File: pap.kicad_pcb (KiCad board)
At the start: 2 copper layers, 60 x 60 mm, 72 parts, among them J51 Conn_01x04, J52 Conn_01x02, J53 Conn_01x02, J54 RJ45, J55 RJ45, J56 RJ12, U1 powerstep01

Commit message: agreo fabricante y algun detalle menor en pcb
solo agrego unos detalles en fab de pcb indicando vias, pistas y
tecnologia de fabricacion. algo tenia, completo algun detalle mas
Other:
- board text added: "AllPCB Fab ********************************** Silkscreen Top White ------------------------- Solder Mask Top Green ------------------------- TOP 2Oz HASL ------------------------- FR4 1.6mm ------------------------- Bottom 2 Oz HASL ------------------------- Solder Mask Bottom Green ------------------------- Silkscreen Bottom White ------------------------- Paste Mask Bottom *********************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"
- board text removed: "Paste Mask Top ------------------------- Silkscreen Top ------------------------- Solder Mask Top ------------------------- TOP 2Oz ------------------------- FR4 1.6mm ------------------------- Bottom 2 Oz ------------------------- Solder Mask Bottom ------------------------- Silkscreen Bottom ------------------------- Paste Mask Bottom -------------------------"
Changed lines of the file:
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@@
   )
   (setup
-    (last_trace_width 1)
+    (last_trace_width 0.2)
     (user_trace_width 0.2)
     (user_trace_width 0.4)
@@
   (gr_line (start 90.83031 137.749079) (end 154.83031 137.749079) (layer Eco2.User) (width 0.3))
   (gr_line (start 90.83031 87.749079) (end 90.83031 137.749079) (layer Eco2.User) (width 0.3))
-  (gr_text "Paste Mask Top\n-------------------------\nSilkscreen Top\n-------------------------\nSolder Mask Top\n-------------------------\nTOP 2Oz\n-------------------------\nFR4 1.6mm\n-------------------------\nBottom 2 Oz\n-------------------------\nSolder Mask Bottom\n-------------------------\nSilkscreen Bottom\n-------------------------\nPaste Mask Bottom\n-------------------------" (at 188.18031 113.579079) (layer F.Fab)
+  (gr_text "AllPCB Fab\n**********************************\n\n\nSilkscreen Top White\n-------------------------\nSolder Mask Top Green\n-------------------------\nTOP 2Oz HASL\n-------------------------\nFR4 1.6mm\n-------------------------\nBottom 2 Oz HASL\n-------------------------\nSolder Mask Bottom Green\n-------------------------\nSilkscreen Bottom White\n-------------------------\nPaste Mask Bottom\n\n**************************************\nTrace/space = 0.25/0.25 mm\n**************************************\nVias Drill/Pad = 0.4/0.8mm\n**************************************" (at 187.23031 112.149079) (layer F.Fab)
     (effects (font (size 1.5 1.5) (thickness 0.3)) (justify left))
   )

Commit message: reviso y ajusto minimo track global a 0.25
en realidad el iC requiere de track de 0.2, pero el resto de la placa
intento llegar a 0.25 para tecnologia de 10/10 mils, y generalmente se
acepta que para el integrado sea un poco mayor que para el ruteo.
veremos.. lo dejo en 0.25/0.25
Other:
- net class Default: trace_width 0.2 -> 0.25
- rule trace_min: 0.2 -> 0.25
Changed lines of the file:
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@@
   )
   (setup
-    (last_trace_width 0.2)
-    (user_trace_width 0.2)
+    (last_trace_width 0.25)
+    (user_trace_width 0.25)
     (user_trace_width 0.4)
     (user_trace_width 0.8)
@@
     (zone_clearance 0.8)
     (zone_45_only yes)
-    (trace_min 0.2)
+    (trace_min 0.25)
     (segment_width 0.3)
     (edge_width 0.15)
@@
   (net_class Default "This is the default net class."
     (clearance 0.25)
-    (trace_width 0.2)
+    (trace_width 0.25)
     (via_dia 1)
     (via_drill 0.5)

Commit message: agfego valores faltantes de capas
Gracias al aporte de Gonzalo, me habian quedado algunos capas sin valor.
.Corrijo. Hay otras sugerencias de Gonzalo que no se corrigen, solo se
consideran y se evaluaran luego
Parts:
- C10, C11, C2, C7, C8: value C -> 100n
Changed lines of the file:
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@@
   (layers
     (0 F.Cu signal)
-    (31 B.Cu signal)
+    (31 B.Cu signal hide)
     (32 B.Adhes user hide)
     (33 F.Adhes user hide)
     (34 B.Paste user hide)
     (35 F.Paste user hide)
-    (36 B.SilkS user)
-    (37 F.SilkS user)
-    (38 B.Mask user)
-    (39 F.Mask user)
+    (36 B.SilkS user hide)
+    (37 F.SilkS user hide)
+    (38 B.Mask user hide)
+    (39 F.Mask user hide)
     (40 Dwgs.User user hide)
     (41 Cmts.User user hide)
     (42 Eco1.User user hide)
-    (43 Eco2.User user)
-    (44 Edge.Cuts user)
-    (45 Margin user)
+    (43 Eco2.User user hide)
+    (44 Edge.Cuts user hide)
+    (45 Margin user hide)
     (46 B.CrtYd user hide)
     (47 F.CrtYd user hide)
     (48 B.Fab user hide)
-    (49 F.Fab user)
+    (49 F.Fab user hide)
   )
   (setup
@@
       (effects (font (size 0.8 0.8) (thickness 0.2)) (justify mirror))
     )
-    (fp_text value C (at 0 -1.65) (layer B.Fab)
+    (fp_text value 100n (at 0 -1.65) (layer B.Fab)
       (effects (font (size 1 1) (thickness 0.15)) (justify mirror))
     )
@@
       (effects (font (size 0.8 0.8) (thickness 0.2)) (justify mirror))
     )
-    (fp_text value C (at 0 -1.65 180) (layer B.Fab)
+    (fp_text value 100n (at 0 -1.65 180) (layer B.Fab)
       (effects (font (size 1 1) (thickness 0.15)) (justify mirror))
     )
@@
       (effects (font (size 0.8 0.8) (thickness 0.2)) (justify mirror))
     )
-    (fp_text value C (at 0 -1.65 270) (layer B.Fab)
+    (fp_text value 100n (at 0 -1.65 270) (layer B.Fab)
       (effects (font (size 1 1) (thickness 0.15)) (justify mirror))
     )
@@
       (effects (font (size 0.8 0.8) (thickness 0.2)) (justify mirror))
     )
-    (fp_text value C (at 0 -1.65 90) (layer B.Fab)
+    (fp_text value 100n (at 0 -1.65 90) (layer B.Fab)
       (effects (font (size 1 1) (thickness 0.15)) (justify mirror))
     )
@@
       (effects (font (size 0.8 0.8) (thickness 0.2)) (justify mirror))
     )
-    (fp_text value C (at 0 -1.65) (layer B.Fab)
+    (fp_text value 100n (at 0 -1.65) (layer B.Fab)
       (effects (font (size 1 1) (thickness 0.15)) (justify mirror))
     )

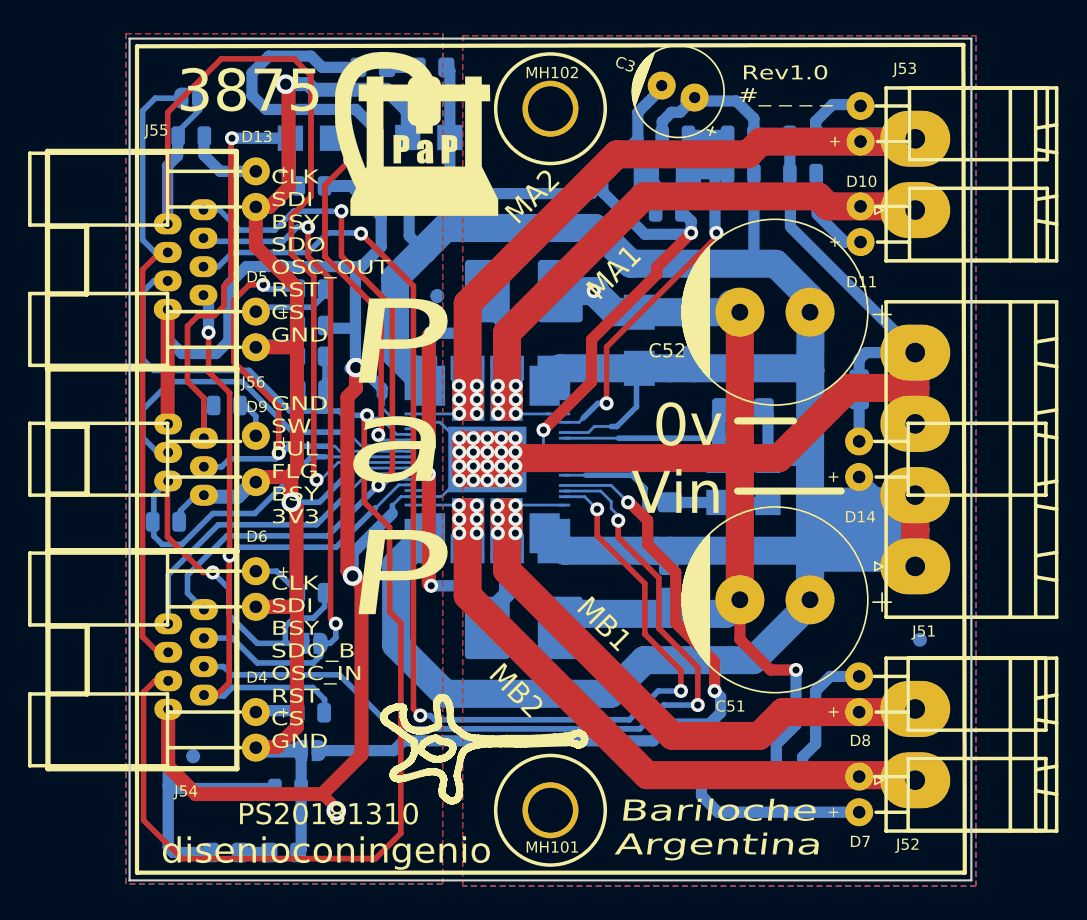
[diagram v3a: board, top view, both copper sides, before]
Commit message: Agrego modelos 3d locales, y corrijo lo solicitado por Diego
Ahi agregue las correcciones que me paso Diego y agregue los modelos 3d
en el repo local que no estaban. el resto fueron ajustes menores.
Tambien agregue las fotos del proto fabricado
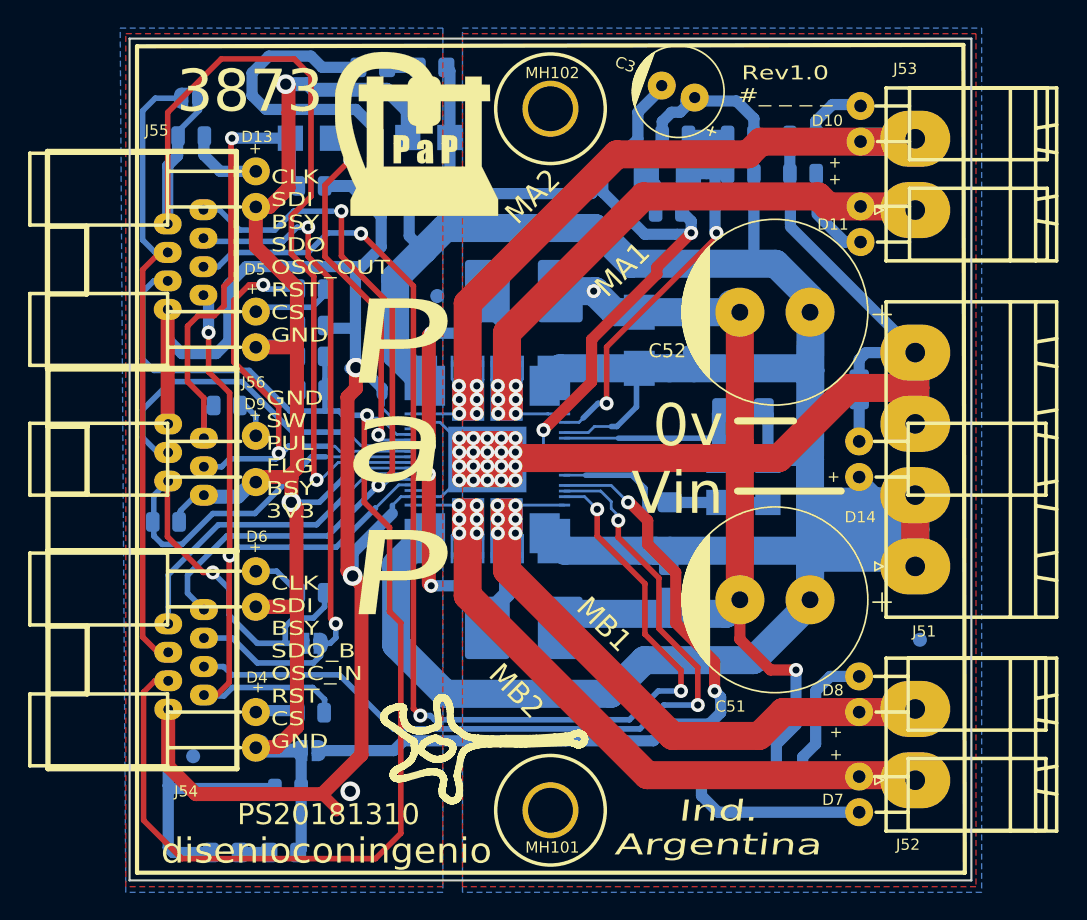
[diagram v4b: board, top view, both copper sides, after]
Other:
- net class Default: clearance 0.25 -> 0.2; trace_width 0.25 -> 0.2
- rule trace_clearance: 0.25 -> 0.2
- rule trace_min: 0.25 -> 0.2
- board text added: "3873"
- board text added: "AllPCB Fab ********************************** Silkscreen Top White ------------------------- Solder Mask Top Green ------------------------- TOP 2Oz HASL ------------------------- FR4 1.6mm ------------------------- Bottom 2 Oz HASL ------------------------- Solder Mask Bottom Green ------------------------- Silkscreen Bottom White ------------------------- Paste Mask Bottom ---------------------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"
- board text added: "Cover these 3 vias below IC with soldermask"
- board text added: "Ind. Argentina"
- board text removed: "AllPCB Fab ********************************** Silkscreen Top White ------------------------- Solder Mask Top Green ------------------------- TOP 2Oz HASL ------------------------- FR4 1.6mm ------------------------- Bottom 2 Oz HASL ------------------------- Solder Mask Bottom Green ------------------------- Silkscreen Bottom White ------------------------- Paste Mask Bottom *********************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"
- board text removed: "Bariloche Argentina"
